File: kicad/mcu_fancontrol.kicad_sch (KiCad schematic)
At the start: 48 parts, among them J1 Vin, J10 NTC1, J11 NTC2, J2 SWIM, J3 UART, J4 Output1, J5 Output2, J6 1-Wire, J7 I2C, J8 I2C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

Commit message: Add new PCB design
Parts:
- added H1, H2: MountingHole, MountingHole:MountingHole_2.7mm_M2.5, symbol Mechanical:MountingHole
- added R13: 3.3k, Resistor_SMD:R_0603_1608Metric, symbol Device:R
- C1: renamed from C2; footprint (none) -> Capacitor_SMD:C_1206_3216Metric
- C10: renamed from C8; footprint (none) -> Capacitor_SMD:C_1206_3216Metric
- C11: renamed from C6; footprint (none) -> Capacitor_SMD:C_0603_1608Metric
- C12: renamed from C7; footprint (none) -> Capacitor_SMD:C_0603_1608Metric
- C13: renamed from C9; footprint (none) -> Capacitor_SMD:C_1206_3216Metric
- C14: renamed from C11; footprint (none) -> Capacitor_SMD:C_1206_3216Metric
- C15: footprint (none) -> Capacitor_SMD:C_0603_1608Metric
- C2: renamed from C1; footprint (none) -> Capacitor_SMD:C_0603_1608Metric
- C3: renamed from C10; footprint (none) -> Capacitor_SMD:C_0603_1608Metric
- C4: renamed from C3; footprint (none) -> Capacitor_SMD:C_0603_1608Metric
- C5: renamed from C12; footprint (none) -> Capacitor_SMD:C_1206_3216Metric
- C6: renamed from C5; footprint (none) -> Capacitor_SMD:C_0603_1608Metric
- C7: renamed from C4; footprint (none) -> Capacitor_SMD:C_0603_1608Metric
- C8: renamed from C13; footprint (none) -> Capacitor_SMD:C_0603_1608Metric
- C9: renamed from C14; footprint (none) -> Capacitor_SMD:C_0603_1608Metric
- J1: footprint (none) -> Connector_Wire:SolderWire-0.5sqmm_1x02_P4.8mm_D0.9mm_OD2.3mm
- J10: renamed from J5; footprint (none) -> Connector:FanPinHeader_1x04_P2.54mm_Vertical
- J11: footprint (none) -> Connector_PinHeader_2.54mm:PinHeader_1x02_P2.54mm_Vertical
- J2: renamed from J7; footprint (none) -> Connector_PinSocket_2.54mm:PinSocket_1x04_P2.54mm_Vertical
- J3: renamed from J8; footprint (none) -> Connector_PinSocket_2.54mm:PinSocket_1x04_P2.54mm_Vertical
- J4: renamed from J9; footprint (none) -> Connector_PinSocket_2.54mm:PinSocket_1x03_P2.54mm_Vertical
- J5: renamed from J6; footprint (none) -> Connector_PinSocket_2.54mm:PinSocket_1x03_P2.54mm_Vertical
- J6: renamed from J2; footprint (none) -> Connector_PinSocket_2.54mm:PinSocket_1x04_P2.54mm_Vertical
- J7: renamed from J3; footprint (none) -> Connector_PinSocket_2.54mm:PinSocket_1x03_P2.54mm_Vertical
- J8: renamed from J10; footprint (none) -> Connector_PinHeader_2.54mm:PinHeader_1x02_P2.54mm_Vertical
- J9: renamed from J4; footprint (none) -> Connector:FanPinHeader_1x04_P2.54mm_Vertical
- JP1: renamed from JP2; footprint (none) -> Jumper:SolderJumper-2_P1.3mm_Open_RoundedPad1.0x1.5mm
- JP2: renamed from JP1; footprint (none) -> Jumper:SolderJumper-2_P1.3mm_Open_RoundedPad1.0x1.5mm
- L1: footprint (none) -> Inductor_THT:L_Radial_D7.0mm_P3.00mm
- R1: renamed from R4; footprint (none) -> Resistor_SMD:R_0603_1608Metric
- R10, R12: footprint (none) -> Resistor_SMD:R_0603_1608Metric
- R11: renamed from R9; footprint (none) -> Resistor_SMD:R_0603_1608Metric
- R2: renamed from R3; footprint (none) -> Resistor_SMD:R_0603_1608Metric
- R3: renamed from R11; footprint (none) -> Resistor_SMD:R_0603_1608Metric
- R4: renamed from R8; footprint (none) -> Resistor_SMD:R_1206_3216Metric
- R5: renamed from R6; footprint (none) -> Resistor_SMD:R_0603_1608Metric
- R6: renamed from R5; footprint (none) -> Resistor_SMD:R_0603_1608Metric
- R7: renamed from R1; footprint (none) -> Resistor_SMD:R_0603_1608Metric
- R8: renamed from R7; footprint (none) -> Resistor_SMD:R_1206_3216Metric
- R9: renamed from R2; footprint (none) -> Resistor_SMD:R_0603_1608Metric
- renumbered Q2 to Q1, Q1 to Q2, U3 to U1, U1 to U3
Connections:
- net 1_WIRE: now also R13.2
- net GND: now also U3.1 (PD4), U3.10 (PA3), U3.5 (PA1), U3.6 (PA2), U4.9 (PAD)
- net V5_33: now also R13.1
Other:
- moved on the sheet: C1, C10, C11, C12, C13, C14, C15, C2, C3, C5, C8, C9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

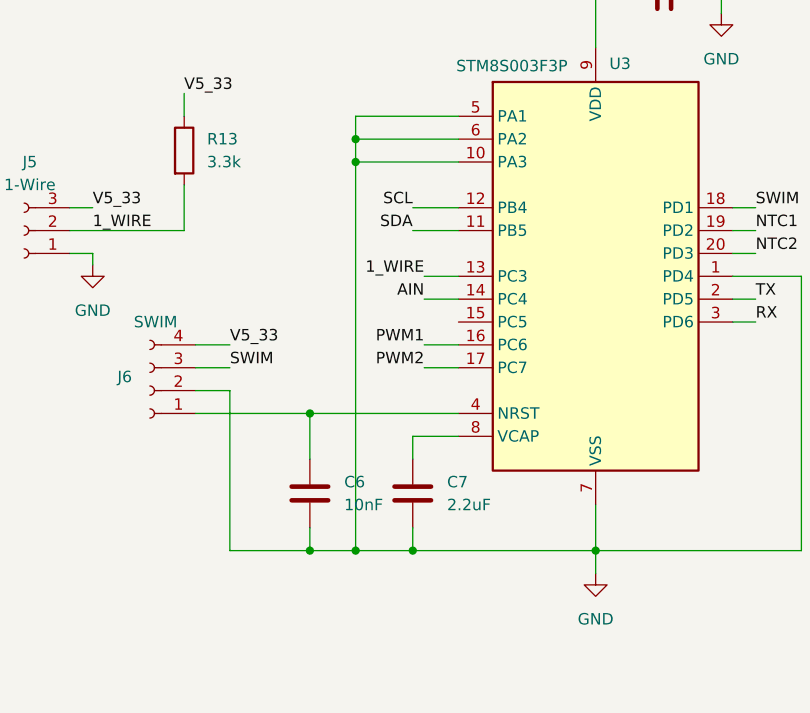
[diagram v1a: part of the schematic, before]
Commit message: pcb: Add teadrops, round tracks
Other minor fixes
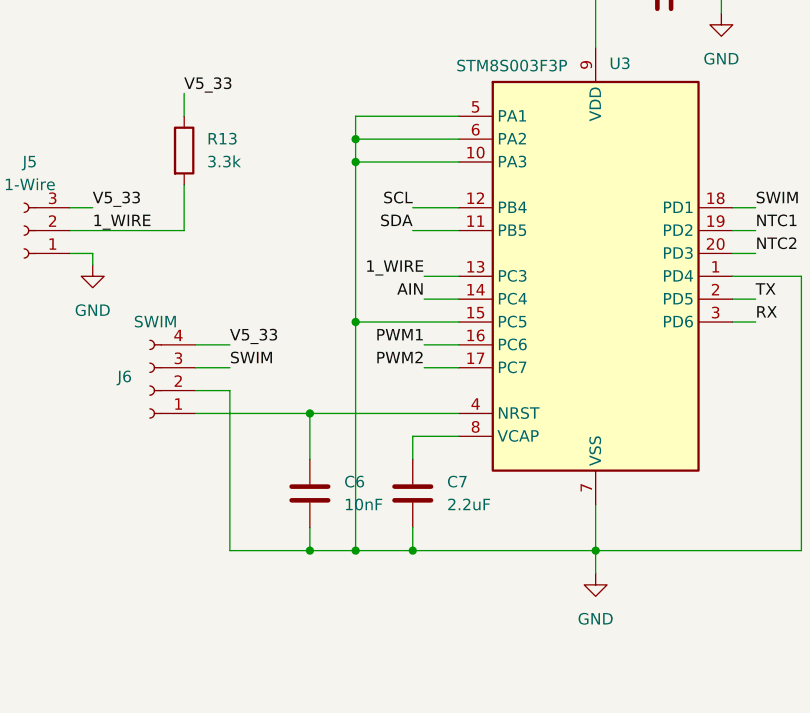
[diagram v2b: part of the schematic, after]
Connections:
- net GND: now also U3.15 (PC5)
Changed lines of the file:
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@@
+	)
+	(junction
+		(at 158.75 127)
+		(diameter 0)
+		(color 0 0 0 0)
 	)
 	(junction
@@
 	(wire
 		(pts
+			(xy 158.75 127) (xy 158.75 152.4)
+		)
+		(stroke
+			(width 0)
+			(type default)
+		)
+	)
+	(wire
+		(pts
 			(xy 302.26 63.5) (xy 308.61 63.5)
 		)
@@
 	(wire
 		(pts
-			(xy 158.75 109.22) (xy 158.75 152.4)
+			(xy 158.75 109.22) (xy 158.75 127)
 		)
 		(stroke
@@
 		)
 		(stroke
+			(width 0)
+			(type default)
+		)
+	)
+	(wire
+		(pts
+			(xy 158.75 127) (xy 170.18 127)
+		)
+		(stroke

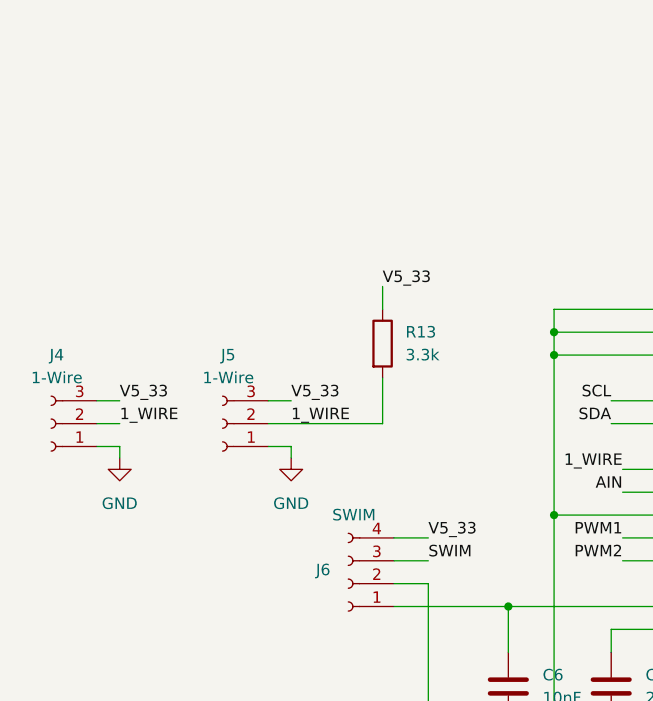
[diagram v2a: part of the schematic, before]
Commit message: pcb: Add optional RC filter for 1-Wire
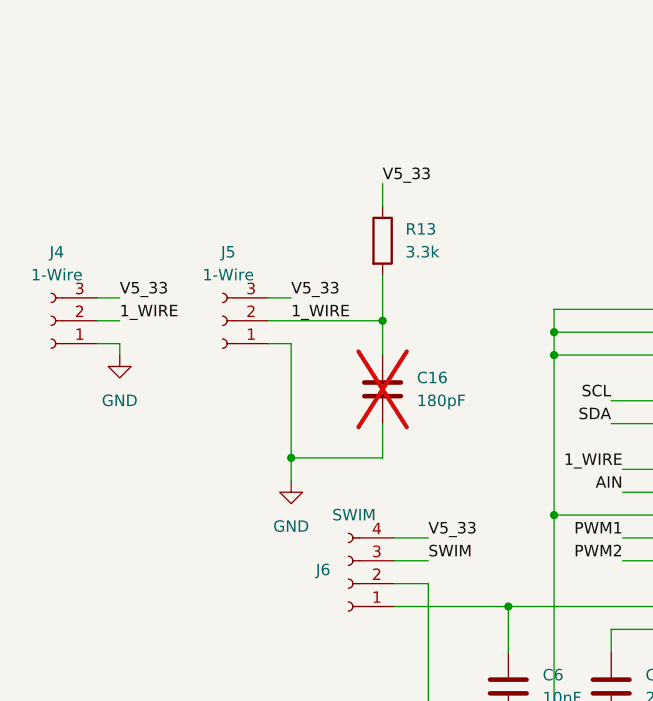
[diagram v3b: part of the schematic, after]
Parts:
- added C16: 180pF, Capacitor_SMD:C_0402_1005Metric_Pad0.74x0.62mm_HandSolder, symbol Device:C
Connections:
- net 1_WIRE: now also C16.1
- net GND: now also C16.2
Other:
- moved on the sheet: J4, J5, R13
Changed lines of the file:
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@@
 	)
 	(junction
+		(at 139.7 105.41)
+		(diameter 0)
+		(color 0 0 0 0)
+	)
+	(junction
 		(at 245.11 69.85)
 		(diameter 0)
@@
 	)
 	(junction
+		(at 129.54 120.65)
+		(diameter 0)
+		(color 0 0 0 0)
+	)
+	(junction
 		(at 147.32 214.63)
 		(diameter 0)
@@
 	(wire
 		(pts
+			(xy 139.7 120.65) (xy 129.54 120.65)
+		)
+		(stroke
+			(width 0)
+			(type default)
+		)
+	)
+	(wire
+		(pts
 			(xy 331.47 156.21) (xy 331.47 146.05)
 		)
@@
 	(wire
 		(pts
-			(xy 127 116.84) (xy 139.7 116.84)
+			(xy 127 105.41) (xy 139.7 105.41)
 		)
 		(stroke
@@
 	(wire
 		(pts
-			(xy 139.7 111.76) (xy 139.7 116.84)
+			(xy 139.7 100.33) (xy 139.7 105.41)
 		)
 		(stroke
@@
 	(wire
 		(pts
-			(xy 107.95 114.3) (xy 110.49 114.3)
+			(xy 107.95 102.87) (xy 110.49 102.87)
 		)
 		(stroke
@@
 	(wire
 		(pts
-			(xy 127 119.38) (xy 129.54 119.38)
+			(xy 129.54 107.95) (xy 127 107.95)
 		)
 		(stroke
@@
 	(wire
 		(pts
+			(xy 129.54 120.65) (xy 129.54 123.19)
+		)
+		(stroke
+			(width 0)
+			(type default)
+		)
+	)
+	(wire
+		(pts
 			(xy 224.79 217.17) (xy 224.79 220.98)
 		)
@@
 	(wire
 		(pts
-			(xy 129.54 119.38) (xy 129.54 120.65)
+			(xy 129.54 107.95) (xy 129.54 120.65)
 		)
 		(stroke
@@
 	(wire
 		(pts
+			(xy 139.7 116.84) (xy 139.7 120.65)
+		)
+		(stroke
+			(width 0)
+			(type default)
+		)
+	)
+	(wire
+		(pts
 			(xy 140.97 137.16) (xy 153.67 137.16)
 		)
@@
 	(wire
 		(pts
-			(xy 107.95 119.38) (xy 110.49 119.38)
+			(xy 107.95 107.95) (xy 110.49 107.95)
 		)
 		(stroke
@@
 	(wire
 		(pts
-			(xy 139.7 101.6) (xy 139.7 104.14)
+			(xy 139.7 90.17) (xy 139.7 92.71)
 		)
 		(stroke
@@
 	(wire
 		(pts
-			(xy 110.49 119.38) (xy 110.49 120.65)
+			(xy 110.49 107.95) (xy 110.49 109.22)
 		)
 		(stroke
@@
 	(wire
 		(pts
-			(xy 107.95 116.84) (xy 110.49 116.84)
+			(xy 107.95 105.41) (xy 110.49 105.41)
 		)
 		(stroke
@@
 	(wire
 		(pts
+			(xy 139.7 105.41) (xy 139.7 109.22)
+		)
+		(stroke
+			(width 0)
+			(type default)
+		)
+	)
+	(wire
+		(pts
 			(xy 330.2 44.45) (xy 330.2 52.07)
 		)
@@
 	(wire
 		(pts
-			(xy 127 114.3) (xy 129.54 114.3)
+			(xy 127 102.87) (xy 129.54 102.87)
 		)
 		(stroke
@@
 	)
 	(label "V5_33"
-		(at 139.7 101.6 0)
+		(at 139.7 90.17 0)
 		(fields_autoplaced yes)
 		(effects
@@
 	)
 	(label "1_WIRE"
-		(at 110.49 116.84 0)
+		(at 110.49 105.41 0)
 		(fields_autoplaced yes)
 		(effects
@@
 	)
 	(label "1_WIRE"
-		(at 129.54 116.84 0)
+		(at 129.54 105.41 0)
 		(fields_autoplaced yes)
 		(effects
@@
 	)
 	(label "V5_33"
-		(at 129.54 114.3 0)
+		(at 129.54 102.87 0)
 		(fields_autoplaced yes)
 		(effects
@@
 	)
 	(label "V5_33"
-		(at 110.49 114.3 0)
+		(at 110.49 102.87 0)
 		(fields_autoplaced yes)
 		(effects
@@
 	(symbol
 		(lib_id "Connector:Conn_01x03_Socket")
-		(at 102.87 116.84 180)
+		(at 102.87 105.41 180)
 		(unit 1)
 		(exclude_from_sim no)
@@
 		(fields_autoplaced yes)
 		(property "Reference" "J4"
-			(at 103.505 109.22 0)
+			(at 103.505 97.79 0)
 			(effects
 				(font
@@
 		)
 		(property "Value" "1-Wire"
-			(at 103.505 111.76 0)
+			(at 103.505 100.33 0)
 			(effects
 				(font
@@
 		)
 		(property "Footprint" "Connector_PinSocket_2.54mm:PinSocket_1x03_P2.54mm_Vertical"
-			(at 102.87 116.84 0)
+			(at 102.87 105.41 0)
 			(effects
 				(font
@@
 		)
 		(property "Datasheet" "~"
-			(at 102.87 116.84 0)
+			(at 102.87 105.41 0)
 			(effects
 				(font
@@
 		)
 		(property "Description" "Generic connector, single row, 01x03, script generated"
-			(at 102.87 116.84 0)
+			(at 102.87 105.41 0)
 			(effects
 				(font
@@
 	(symbol
 		(lib_id "Device:R")
-		(at 139.7 107.95 0)
+		(at 139.7 96.52 0)
 		(unit 1)
 		(exclude_from_sim no)
@@
 		(fields_autoplaced yes)
 		(property "Reference" "R13"
-			(at 142.24 106.6799 0)
+			(at 142.24 95.2499 0)
 			(effects
 				(font
@@
 		)
 		(property "Value" "3.3k"
-			(at 142.24 109.2199 0)
+			(at 142.24 97.7899 0)
 			(effects
 				(font
@@
 		)
 		(property "Footprint" "Resistor_SMD:R_0603_1608Metric"
-			(at 137.922 107.95 90)
+			(at 137.922 96.52 90)
 			(effects
 				(font
@@
 		)
 		(property "Datasheet" "~"
-			(at 139.7 107.95 0)
+			(at 139.7 96.52 0)
 			(effects
 				(font
@@
 		)
 		(property "Description" "Resistor"
-			(at 139.7 107.95 0)
+			(at 139.7 96.52 0)
 			(effects
 				(font
@@
 	(symbol
 		(lib_id "power:GND")
-		(at 129.54 120.65 0)
+		(at 129.54 123.19 0)
 		(unit 1)
 		(exclude_from_sim no)
@@
 		(fields_autoplaced yes)
 		(property "Reference" "#PWR05"
-			(at 129.54 127 0)
+			(at 129.54 129.54 0)
 			(effects
 				(font
@@
 		)
 		(property "Value" "GND"
-			(at 129.54 125.73 0)
+			(at 129.54 128.27 0)
 			(effects
 				(font
@@
 		)
 		(property "Footprint" ""
-			(at 129.54 120.65 0)
+			(at 129.54 123.19 0)
 			(effects
 				(font
@@
 		)
 		(property "Datasheet" ""
-			(at 129.54 120.65 0)
+			(at 129.54 123.19 0)
 			(effects
 				(font
@@
 		)
 		(property "Description" "Power symbol creates a global label with name \"GND\" , ground"
-			(at 129.54 120.65 0)
+			(at 129.54 123.19 0)
 			(effects
 				(font
@@
 	(symbol
 		(lib_id "Connector:Conn_01x03_Socket")
-		(at 121.92 116.84 180)
+		(at 121.92 105.41 180)
 		(unit 1)
 		(exclude_from_sim no)
@@
 		(fields_autoplaced yes)
 		(property "Reference" "J5"
-			(at 122.555 109.22 0)
+			(at 122.555 97.79 0)
 			(effects
 				(font
@@
 		)
 		(property "Value" "1-Wire"
-			(at 122.555 111.76 0)
+			(at 122.555 100.33 0)
 			(effects
 				(font
@@
 		)
 		(property "Footprint" "Connector_PinSocket_2.54mm:PinSocket_1x03_P2.54mm_Vertical"
-			(at 121.92 116.84 0)
+			(at 121.92 105.41 0)
 			(effects
 				(font
@@
 		)
 		(property "Datasheet" "~"
-			(at 121.92 116.84 0)
+			(at 121.92 105.41 0)
 			(effects
 				(font
@@
 		)
 		(property "Description" "Generic connector, single row, 01x03, script generated"
-			(at 121.92 116.84 0)
+			(at 121.92 105.41 0)
 			(effects
 				(font
@@
 	(symbol
 		(lib_id "Device:C")
+		(at 139.7 113.03 0)
+		(unit 1)
+		(exclude_from_sim no)
+		(in_bom yes)
+		(on_board yes)
+		(dnp yes)
+		(fields_autoplaced yes)
+		(property "Reference" "C16"
+			(at 143.51 111.7599 0)
+			(effects
+				(font
+					(size 1.27 1.27)
+				)
+				(justify left)
+			)
+		)
+		(property "Value" "180pF"
+			(at 143.51 114.2999 0)
+			(effects
+				(font
+					(size 1.27 1.27)
+				)
+				(justify left)
+			)
+		)
+		(property "Footprint" "Capacitor_SMD:C_0402_1005Metric_Pad0.74x0.62mm_HandSolder"
+			(at 140.6652 116.84 0)
+			(effects
+				(font
+					(size 1.27 1.27)
+				)
+				(hide yes)
+			)
+		)
+		(property "Datasheet" "~"
+			(at 139.7 113.03 0)
+			(effects
+				(font
+					(size 1.27 1.27)
+				)
+				(hide yes)
+			)
+		)
+		(property "Description" "Unpolarized capacitor"
+			(at 139.7 113.03 0)
+			(effects
+				(font
+					(size 1.27 1.27)
+				)
+				(hide yes)
+			)
+		)
+		(pin "2"
+		)
+		(pin "1"
+		)
+		(instances
+			(project "mcu_fancontrol"
+				(path "/59a9ff8c-88b2-4148-b805-385246301469"
+					(reference "C16")
+					(unit 1)
+				)
+			)
+		)
+	)
+	(symbol
+		(lib_id "Device:C")
 		(at 331.47 139.7 0)
 		(unit 1)
@@
 	(symbol
 		(lib_id "power:GND")
-		(at 110.49 120.65 0)
+		(at 110.49 109.22 0)
 		(unit 1)
 		(exclude_from_sim no)
@@
 		(fields_autoplaced yes)
 		(property "Reference" "#PWR04"
-			(at 110.49 127 0)
+			(at 110.49 115.57 0)
 			(effects
 				(font
@@
 		)
 		(property "Value" "GND"
-			(at 110.49 125.73 0)
+			(at 110.49 114.3 0)
 			(effects
 				(font
@@
 		)
 		(property "Footprint" ""
-			(at 110.49 120.65 0)
+			(at 110.49 109.22 0)
 			(effects
 				(font
@@
 		)
 		(property "Datasheet" ""
-			(at 110.49 120.65 0)
+			(at 110.49 109.22 0)
 			(effects
 				(font
@@
 		)
 		(property "Description" "Power symbol creates a global label with name \"GND\" , ground"
-			(at 110.49 120.65 0)
+			(at 110.49 109.22 0)
 			(effects
 				(font
